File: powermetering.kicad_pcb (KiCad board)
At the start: 2 copper layers, 194 x 114.1 mm, 237 parts, among them J1 Conn_01x04, J10 Micro_SD_Card, J16 Conn_02x20_Odd_Even, J2 Conn_01x02, J3 Conn_01x02, J4 Conn_01x02, J5 Conn_01x02, J6 HY951180A_RJ45, J7 CONN_01X02, J9 CONN_01X02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

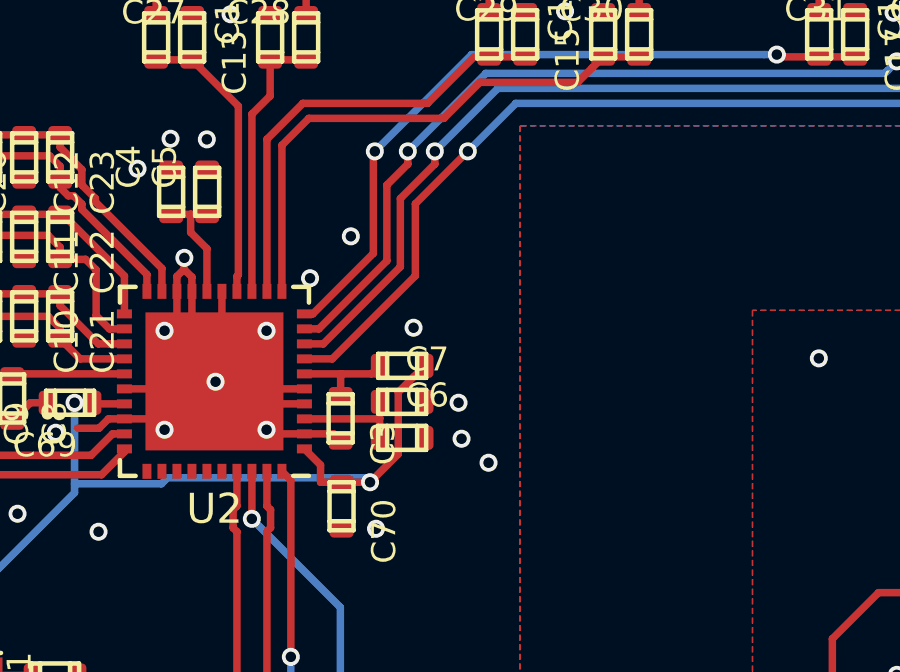
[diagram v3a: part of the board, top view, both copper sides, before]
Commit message: add ade reset jumper
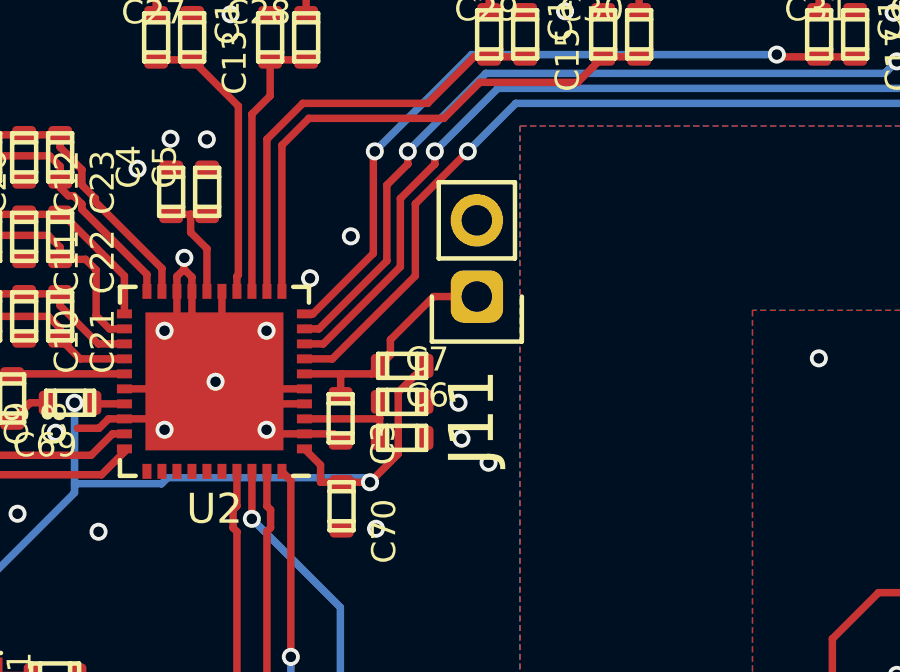
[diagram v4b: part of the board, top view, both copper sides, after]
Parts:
- added J11: CONN_01X02, stmbl:Pin_Header_Straight_1x02, F.Cu at (218.2, 99.7)
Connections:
- net /PHY_TXD0 renamed /STM_TXD0
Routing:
- net /RESET: track 3.36 -> 7.85 mm
- net N: vias 39 -> 38

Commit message: small changes
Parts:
- added C76: 100n, stmbl:C_0805, F.Cu at (197.3, 200.2)
- added H1: MountingHole, MountingHole:MountingHole_3.2mm_M3, F.Cu at (199.1, 186.9)
- added H12: MountingHole, MountingHole:MountingHole_3.2mm_M3, F.Cu at (214.9, 186.9)
- added H13: MountingHole, MountingHole:MountingHole_3.2mm_M3, F.Cu at (214.9, 194.9)
- added H15: MountingHole, MountingHole:MountingHole_3.2mm_M3, F.Cu at (222.9, 186.9)
- added H2: MountingHole, MountingHole:MountingHole_3.2mm_M3, F.Cu at (199.1, 194.9)
- added H3: MountingHole, MountingHole:MountingHole_3.2mm_M3, F.Cu at (207.0, 186.9)
- added H4: MountingHole, MountingHole:MountingHole_3.2mm_M3, F.Cu at (207.0, 194.9)
- added J12: CONN_01X02, stmbl:Pin_Header_Straight_1x02, F.Cu at (229.2, 185.2)
- added J13: CONN_01X02, stmbl:Pin_Header_Straight_1x02, F.Cu at (221.2, 200.2)
- added J14: CONN_01X02, stmbl:Pin_Header_Straight_1x02, F.Cu at (225.8, 193.2)
- added J15: CONN_01X02, stmbl:Pin_Header_Straight_1x02, F.Cu at (230.3, 192.3)
- added J8: CONN_01X02, stmbl:Pin_Header_Straight_1x02, F.Cu at (221.2, 193.2)
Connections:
- net /PHY_TXD1 renamed /STM_TXD1
- net /STM_TXD0 renamed /PHY_TXD0
- D21 pad 3: L3 -> GNDS
- D21 pad 4: L2 -> L3
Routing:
- net GNDS: track 53.4 -> 75.4 mm
- net L3: track 43.4 -> 47.5 mm, vias 0 -> 1
- net L2: track 58.3 -> 56.8 mm
- net GNDPWR: vias 19 -> 20
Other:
- board text added: "V3"
- board text removed: "V2"

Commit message: small production changes
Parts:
- removed C28, C29, C30, C31, C32, C33, C34: C, stmbl:C_0603
- removed C76: 100n, stmbl:C_0805
- removed D1: LED, stmbl-kicad-lib:LED-0805
- removed H1, H12, H13, H15, H2, H3, H4: MountingHole, MountingHole:MountingHole_3.2mm_M3
- removed J12, J13, J14, J15, J8: CONN_01X02, stmbl:Pin_Header_Straight_1x02
- removed R14, R15, R16, R17, R18, R19, R20, R21: 1k, stmbl:R_0603
- removed R2: R, stmbl:R_0603
- C27: value C -> 470µ; footprint stmbl:C_0603 -> Capacitor_SMD:CP_Elec_6.3x5.9
- H10, H11, H14, H16, H9: footprint MountingHole:MountingHole_3.2mm_M3 -> MountingHole:MountingHole_5.5mm
- J1: footprint TerminalBlock_Phoenix:TerminalBlock_Phoenix_PT-1,5-5-5.0-H_1x05_P5.00mm_Horizontal -> stmbl:RM5.08_1x5_UP
- J2, J3, J4, J5: footprint TerminalBlock_Phoenix:TerminalBlock_Phoenix_PT-1,5-2-5.0-H_1x02_P5.00mm_Horizontal -> stmbl:RM5.08_1x2_UP
- R10, R11, R12, R13, R6, R7, R8, R9: value 0R -> 1k
- R25, R26, R27, R28, R29, R30, R31, R32, R33, R42, R43, R44: footprint Resistor_SMD:R_2010_5025Metric -> stmbl:R_1206
- moved C27 21.8 mm to (204.8, 110.4)
- moved J2 6.63 mm to (204.8, 74.5)
- moved J3 6.24 mm to (217.2, 74.5)
- moved J5 6.24 mm to (242.0, 74.5)
- moved J4 6.10 mm to (229.6, 74.5)
- moved D4 4.30 mm to (219.1, 87.4)
- moved D5 4.30 mm to (223.0, 87.4)
- moved D2 4.30 mm to (208.2, 87.5)
- moved D3 4.30 mm to (211.8, 87.5)
- moved D6 4.30 mm to (230.2, 87.5)
- moved D7 4.30 mm to (234.0, 87.5)
- moved D8 4.30 mm to (241.3, 87.5)
- moved D9 4.30 mm to (245.2, 87.5)
- moved R34 4.30 mm to (207.9, 81.8)
- moved R35 4.30 mm to (212.1, 81.8)
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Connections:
- net /PHY_MDC renamed /STM_MDC
- net /PHY_REFCLK renamed /STM_REFCLK
- net /PHY_RXD0 renamed /STM_RXD0
- net /PHY_RXD1 renamed /STM_RXD1
- net /PHY_TXEN renamed /STM_TXEN
- net /STM_CRS renamed /PHY_CRS
- C27 pad 1: Net-(C27-Pad1) -> +3.3VA
- J6 pad 8: Net-(J6-Pad8) -> GND
- R10 pad 2: Net-(C31-Pad1) -> Net-(D6-Pad1)
- R11 pad 2: Net-(C32-Pad2) -> Net-(D7-Pad1)
- R12 pad 2: Net-(C33-Pad1) -> Net-(D8-Pad1)
- R13 pad 2: Net-(C34-Pad2) -> Net-(D9-Pad1)
- R6 pad 2: Net-(C27-Pad1) -> Net-(D2-Pad1)
- R7 pad 2: Net-(C28-Pad2) -> Net-(D3-Pad1)
- R8 pad 2: Net-(C29-Pad1) -> Net-(D4-Pad1)
- R9 pad 2: Net-(C30-Pad2) -> Net-(D5-Pad1)
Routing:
- net Net-(C34-Pad2): track 3.00 -> 0.00 mm
- net Net-(C32-Pad2): track 3.00 -> 0.00 mm
- net Net-(C31-Pad1): track 3.00 -> 0.00 mm
- net Net-(C28-Pad2): track 3.00 -> 0.00 mm
- net Net-(C27-Pad1): track 3.00 -> 0.00 mm
- net Net-(C33-Pad1): track 3.00 -> 0.00 mm
- net Net-(C30-Pad2): track 3.00 -> 0.00 mm
- net Net-(C29-Pad1): track 3.00 -> 0.00 mm
- net Net-(D7-Pad1): track 17.7 -> 15.8 mm
- net Net-(D6-Pad1): track 17.7 -> 15.9 mm
- net Net-(D9-Pad1): track 17.7 -> 16.1 mm
- net Net-(D1-Pad1): track 1.60 -> 0.00 mm
- net Net-(D4-Pad1): track 17.7 -> 16.1 mm
- net Net-(R32-Pad1): track 4.56 -> 6.06 mm
- net Net-(R31-Pad1): track 4.06 -> 5.56 mm
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
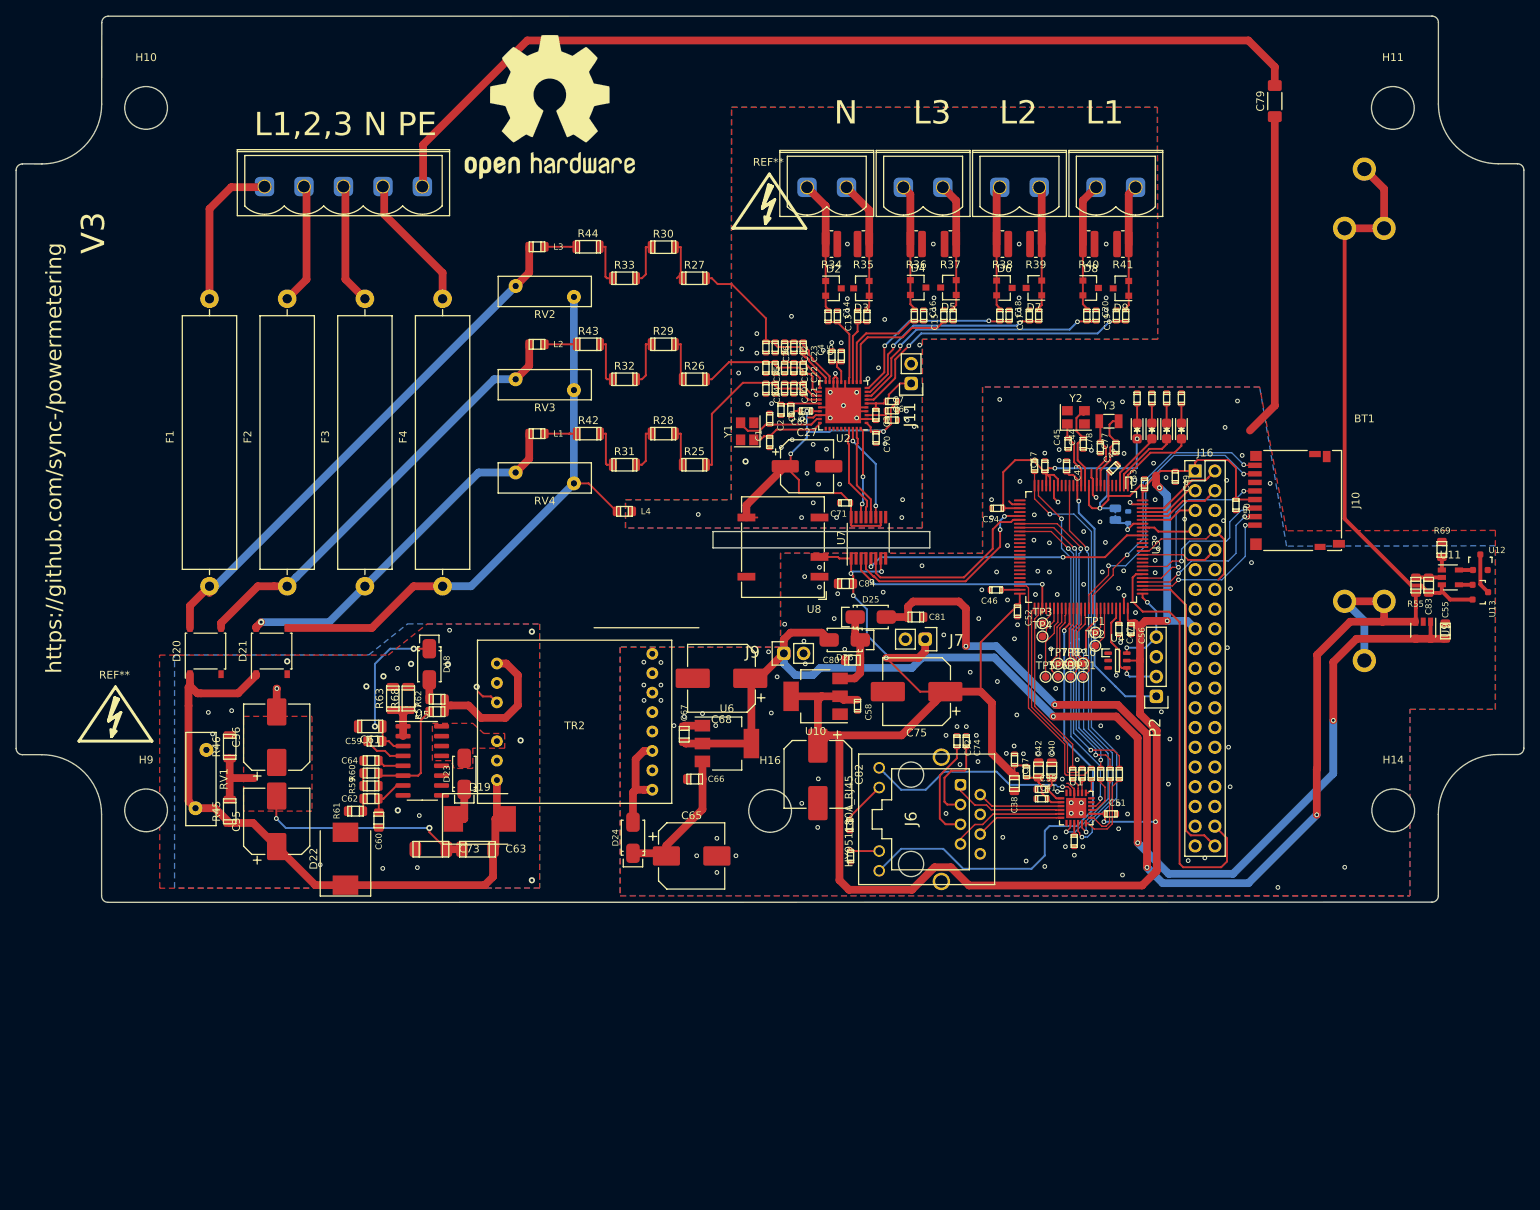
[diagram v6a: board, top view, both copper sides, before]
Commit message: fix SD card socket, move around psu stuff
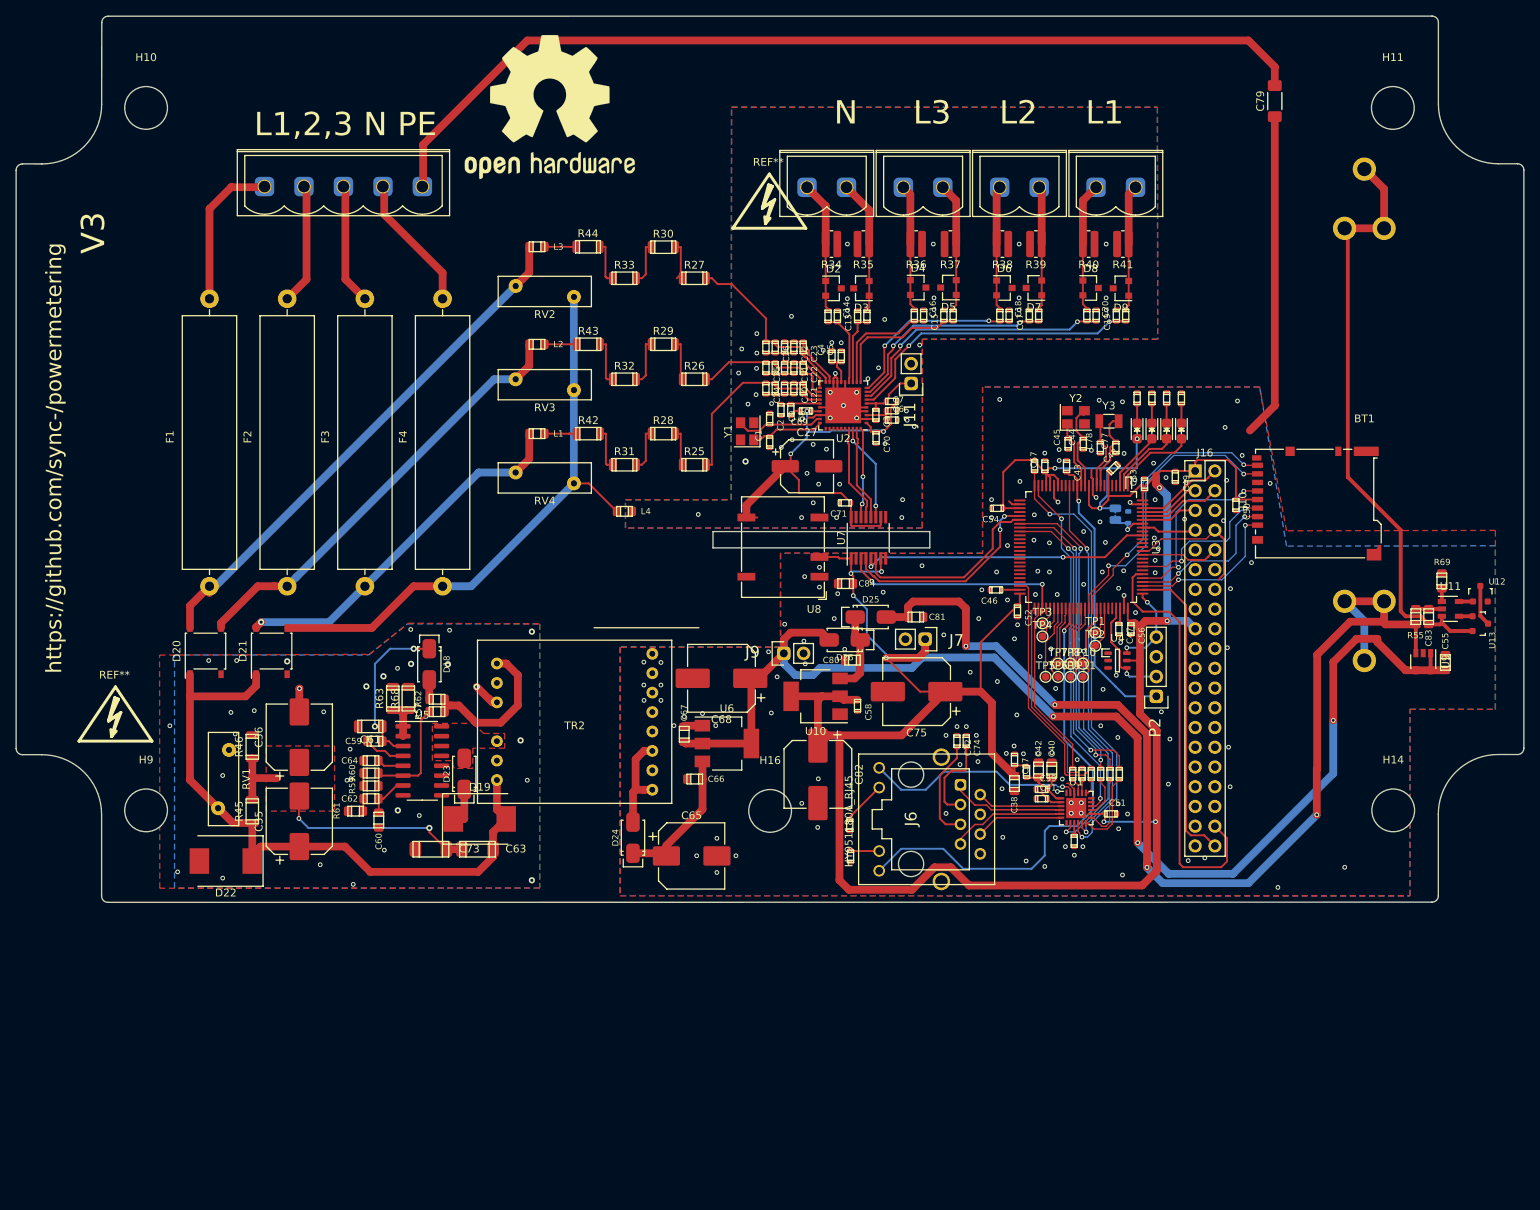
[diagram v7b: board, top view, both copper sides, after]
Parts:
- J10: footprint Connector_Card:microSD_HC_Hirose_DM3D-SF -> Connector_Card:microSD_HC_Hirose_DM3BT-DSF-PEJS
- moved D22 15.4 mm to (130.0, 161.2), turned to 180 degrees
- moved C55 4.05 mm to (286.9, 135.7)
- moved R69 4.05 mm to (286.5, 125.2)
- moved U13 4.05 mm to (291.4, 130.7)
- moved U9 4.05 mm to (284.1, 135.6)
- moved C83 4.05 mm to (284.8, 129.8)
- moved R55 4.05 mm to (283.1, 129.8)
- moved U11 4.05 mm to (287.6, 128.8)
- moved U12 4.05 mm to (291.4, 126.8)
- moved C35 2.91 mm to (139.5, 156.1)
- moved C36 2.91 mm to (139.5, 145.3)
- moved R45 2.91 mm to (133.4, 154.8)
- moved R46 2.91 mm to (133.4, 146.5)
- moved RV1 2.91 mm to (129.0, 154.4)
- moved J10 2.63 mm to (270.4, 115.2), turned to 90 degrees
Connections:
- net /PHY_MDIO renamed /STM_MDIO
- net /STM_REFCLK renamed /PHY_REFCLK
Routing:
- net N: track 20.3 -> 31.1 mm
- net Net-(BT1-Pad2): track 72.9 -> 77.4 mm
- net GNDPWR: track 13.1 -> 16.5 mm, vias 20 -> 31
- net Net-(C35-Pad2): track 37.2 -> 34.3 mm
- net +5V: track 162.4 -> 164.4 mm
- net VPP: track 83.2 -> 84.9 mm
- net Net-(R57-Pad1): track 19.5 -> 20.1 mm

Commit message: remove eight pulse rectifier, add three pulse rectifier with artificial star point
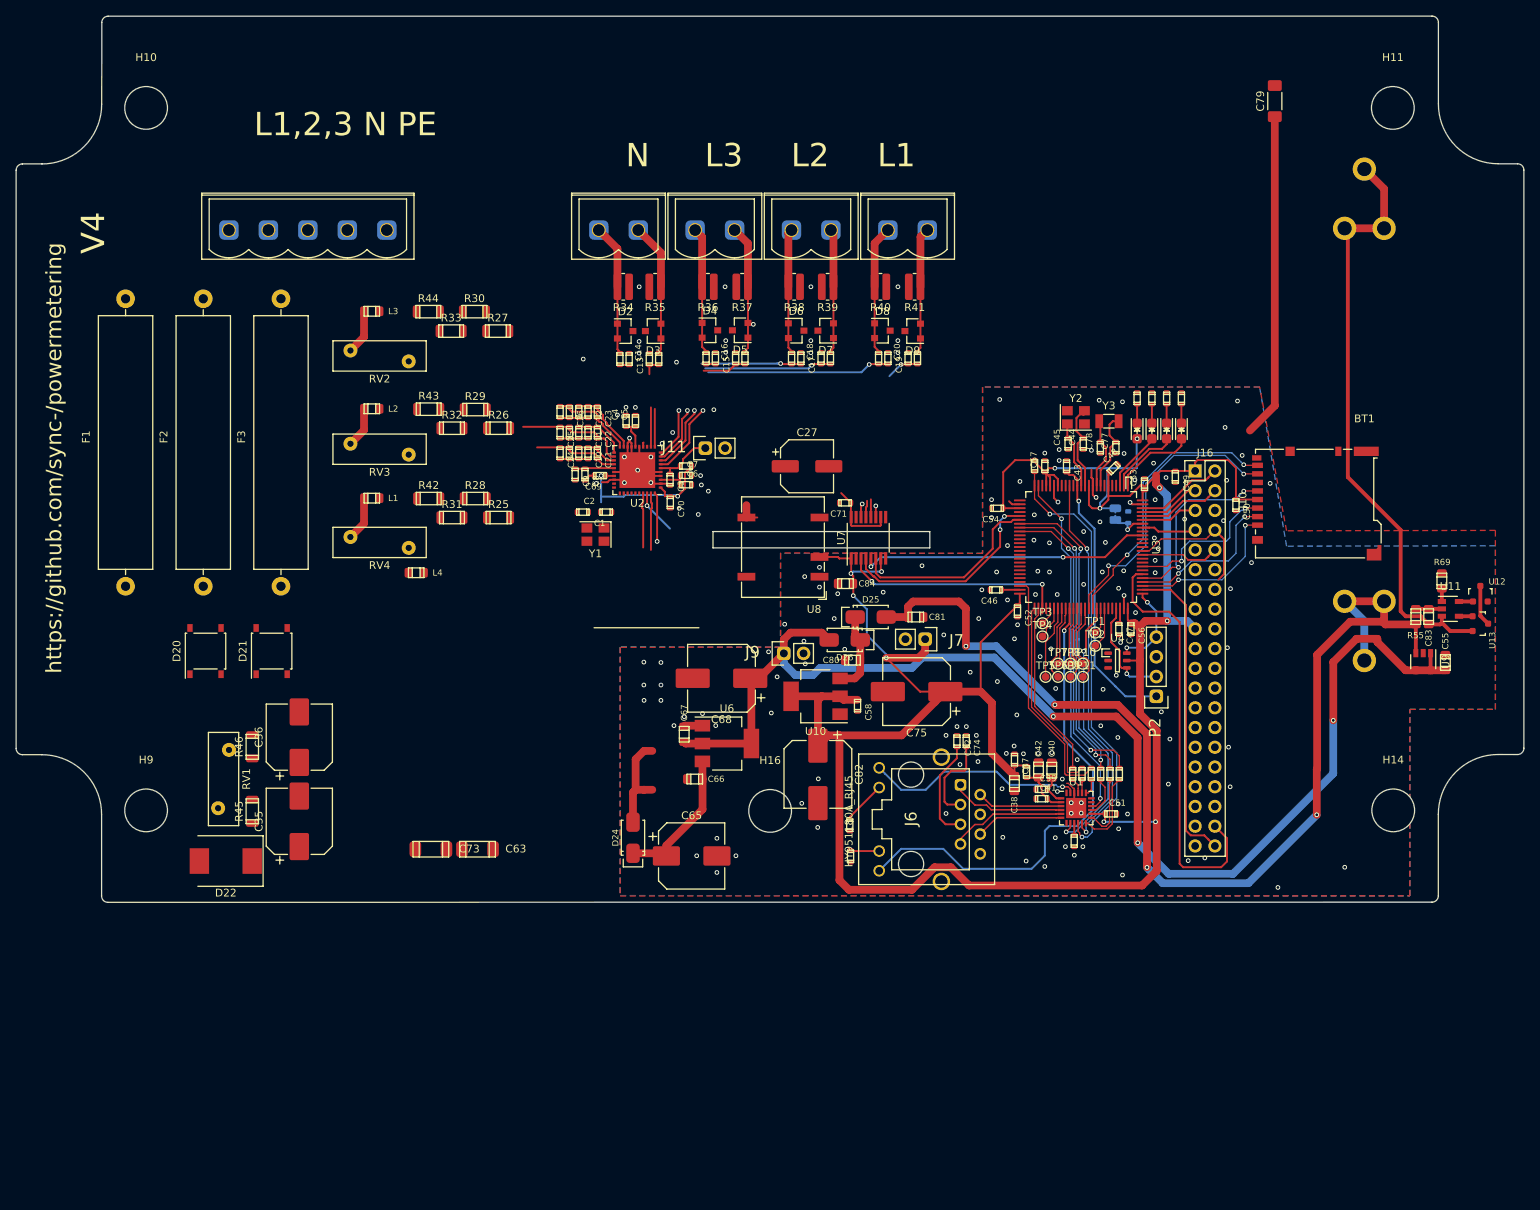
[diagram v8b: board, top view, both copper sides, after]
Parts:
- removed C59: 100n, stmbl:C_0805
- removed C60: 1n, stmbl:C_0805
- removed C61: 2.2µ, stmbl:C_1206
- removed C62: 470n, stmbl:C_0805
- removed C64: 4.7n, stmbl:C_0805
- removed D18, D23: D, stmbl:SMA_Standard
- removed D19: 1.5KExxA, Diode_SMD:D_SMC
- removed F4: Fuse, Fuse:Fuse_SunFuse-6HP
- removed R57: 33k, stmbl:R_0805
- removed R59, R61: 8.2k, stmbl:R_0805
- removed R60: 51k, stmbl:R_0805
- removed R62: 0, stmbl:R_0805
- removed R63: 1.3, stmbl:R_1206
- removed R68: DNP, stmbl:R_1206
- removed REF** (x2): Symbol_HighVoltage_Type2_Top_VerySmall, stmbl:Symbol_HighVoltage_Type2_Top_VerySmall
- removed REF**: OSHW-Logo2_24.3x20mm_SilkScreen, Symbol:OSHW-Logo2_24.3x20mm_SilkScreen
- removed TR2: 750871110, altair04:750871110
- removed U5: ALTAIR04-900, Package_SO:SOIC-16_3.9x9.9mm_P1.27mm
- C1, C2: value C -> 10p
- C3, C5, C69, C7, C70, C71, C9: value C -> 100n
- C4, C6, C8: value C -> 2.2µ
- C79: value C -> 1n
- R1: value R -> 10k
- moved L4 27.9 mm to (154.5, 124.1)
- moved C12 27.8 mm to (176.6, 103.4)
- moved C23 27.8 mm to (177.8, 103.4)
- moved C26 27.8 mm to (174.2, 103.4)
- moved C3 27.8 mm to (187.2, 112.1)
- moved C8 27.8 mm to (176.2, 111.5)
- moved C9 27.8 mm to (175.0, 111.5)
- moved R1 27.8 mm to (189.2, 110.4)
- moved R5 27.8 mm to (175.4, 103.4)
- moved C10 27.8 mm to (176.6, 108.7)
- moved C11 27.8 mm to (176.6, 106.1)
- moved C21 27.8 mm to (177.8, 108.7)
- moved C22 27.8 mm to (177.8, 106.1)
- moved C5 27.8 mm to (182.7, 104.6)
- moved C6 27.8 mm to (189.2, 112.8)
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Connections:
- net /PHY_REFCLK renamed /STM_REFCLK
- net /STM_MDIO renamed /PHY_MDIO
- J1 pad 4: Net-(F4-Pad1) -> GNDS
- U3 pad 6: +3V3 -> Net-(C28-Pad1)
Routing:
- net Earth_Protective: track 124.4 -> 0.00 mm
- net VPP: track 84.9 -> 0.00 mm
- net GNDS: track 75.4 -> 0.00 mm
- net L1: track 68.5 -> 5.77 mm
- net L2: track 56.8 -> 5.22 mm
- net L3: track 47.5 -> 5.72 mm, vias 1 -> 0
- net Net-(C35-Pad2): track 34.3 -> 0.00 mm, vias 2 -> 0
- net /IL1P: track 38.9 -> 14.0 mm
- net /VCC: track 21.6 -> 0.00 mm, vias 2 -> 0
- net +3.3VA: track 56.9 -> 35.3 mm, vias 3 -> 2
- net Net-(F1-Pad1): track 20.2 -> 0.00 mm
- net Net-(R57-Pad1): track 20.1 -> 0.00 mm
- net Net-(F4-Pad1): track 17.5 -> 0.00 mm
- net GNDPWR: track 16.5 -> 0.00 mm, vias 31 -> 0
- net /FB: track 15.7 -> 0.00 mm
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- removed copper zone on F.Cu, net /DRN
- removed copper zone on B.Cu, net GNDPWR
- removed copper zone on F.Cu, net GNDPWR
- removed copper zone on B.Cu, net N
- removed copper zone on F.Cu, net N
- removed copper zone on F.Cu, net Net-(C35-Pad2)
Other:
- board text added: "V4"
- board text removed: "V3"
